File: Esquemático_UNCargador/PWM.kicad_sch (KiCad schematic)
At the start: 10 parts, among them U1 LM324N

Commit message: Se modifica esquema del micro y se agrega página de sensores
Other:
- note added: "VERIFICAR ESTE COMPONENTE"
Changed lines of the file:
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@@
+    (stroke (width 0) (type default))
+  )
+  (wire (pts (xy 85.09 30.48) (xy 86.36 30.48))
     (stroke (width 0) (type default))
   )
@@
     (stroke (width 0) (type default))
   )
-  (wire (pts (xy 85.09 30.48) (xy 85.598 30.48))
-    (stroke (width 0) (type default))
-  )
   (wire (pts (xy 120.65 73.66) (xy 120.65 72.39))
     (stroke (width 0) (type default))
   )
+  (wire (pts (xy 86.36 26.67) (xy 86.36 30.48))
+    (stroke (width 0) (type default))
+  )
   (wire (pts (xy 137.16 58.42) (xy 140.97 58.42))
     (stroke (width 0) (type default))
@@
     (stroke (width 0) (type default))
   )
+  (wire (pts (xy 26.67 59.69) (xy 26.67 70.866))
+    (stroke (width 0) (type default))
+  )
+  (wire (pts (xy 137.16 57.15) (xy 137.16 58.42))
+    (stroke (width 0) (type default))
+  )
+  (wire (pts (xy 140.97 58.42) (xy 149.86 58.42))
+    (stroke (width 0) (type default))
+  )
   (wire (pts (xy 78.74 30.48) (xy 85.09 30.48))
     (stroke (width 0) (type default))
   )
-  (wire (pts (xy 26.67 59.69) (xy 26.67 70.866))
-    (stroke (width 0) (type default))
-  )
-  (wire (pts (xy 137.16 57.15) (xy 137.16 58.42))
-    (stroke (width 0) (type default))
-  )
-  (wire (pts (xy 140.97 58.42) (xy 149.86 58.42))
-    (stroke (width 0) (type default))
-  )
   (wire (pts (xy 104.14 57.15) (xy 137.16 57.15))
     (stroke (width 0) (type default))
@@
   (wire (pts (xy 123.19 73.66) (xy 120.65 73.66))
     (stroke (width 0) (type default))
+  )
+  (text "VERIFICAR \nESTE \nCOMPONENTE" (at 144.78 69.85 0)
+    (effects (font (size 1.2 1.2) (color 255 14 46 1)) (justify left bottom))
   )
   (global_label "Pilot_ADC" (shape output) (at 123.19 73.66 0) (fields_autoplaced)
@@
     )
   )
-  (symbol (lib_id "power:+12V") (at 85.09 30.48 0) (unit 1)
-    (in_bom yes) (on_board yes) (dnp no) (fields_autoplaced)
-    (property "Reference" "#PWR0101" (at 85.09 34.29 0)
-      (effects (font (size 1.27 1.27)) hide)
-    )
-    (property "Value" "+12V" (at 85.09 25.146 0)
-      (effects (font (size 1.27 1.27)))
-    )
-    (property "Footprint" "" (at 85.09 30.48 0)
-      (effects (font (size 1.27 1.27)) hide)
-    )
-    (property "Datasheet" "" (at 85.09 30.48 0)
-      (effects (font (size 1.27 1.27)) hide)
-    )
+  (symbol (lib_id "power:+12V") (at 86.36 26.67 0) (unit 1)
+    (in_bom yes) (on_board yes) (dnp no) (fields_autoplaced)
+    (property "Reference" "#PWR0101" (at 86.36 30.48 0)
+      (effects (font (size 1.27 1.27)) hide)
+    )
+    (property "Value" "+12V" (at 86.36 21.336 0)
+      (effects (font (size 1.27 1.27)))
+    )
+    (property "Footprint" "" (at 86.36 26.67 0)
+      (effects (font (size 1.27 1.27)) hide)
+    )
+    (property "Datasheet" "" (at 86.36 26.67 0)
+      (effects (font (size 1.27 1.27)) hide)
+    )

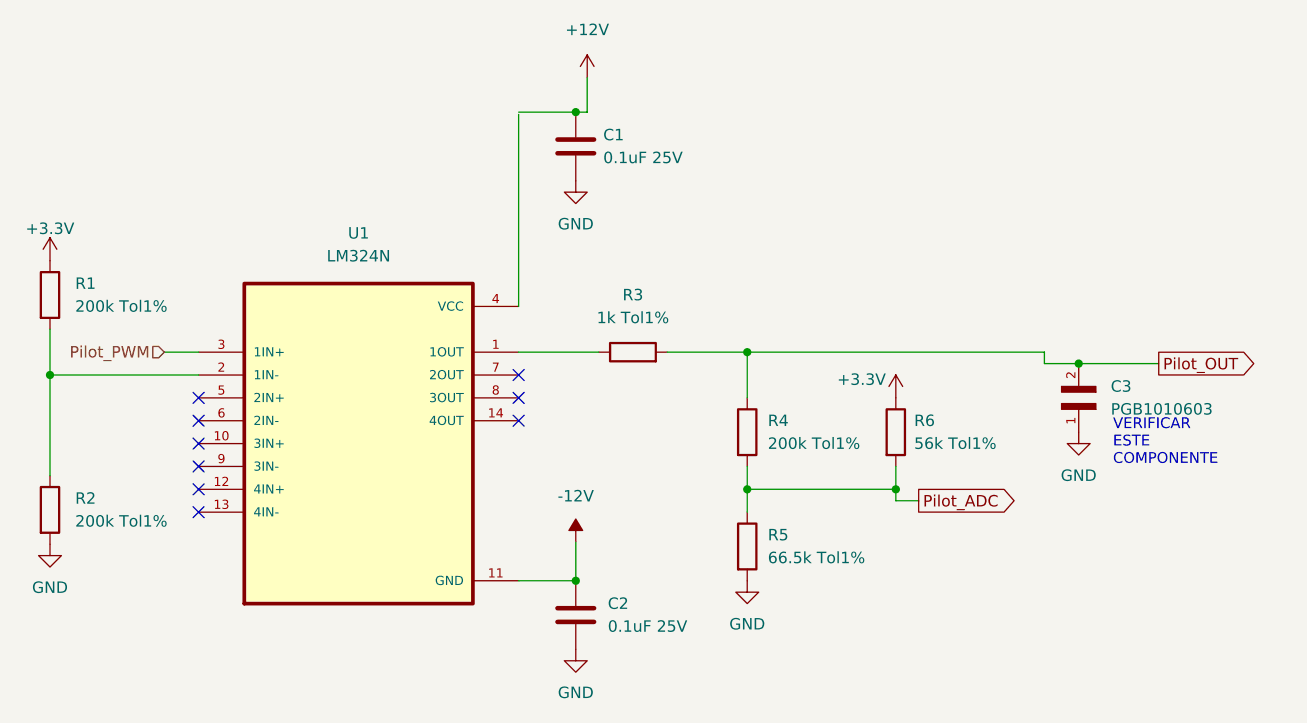
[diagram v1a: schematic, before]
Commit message: Avances en Huellas
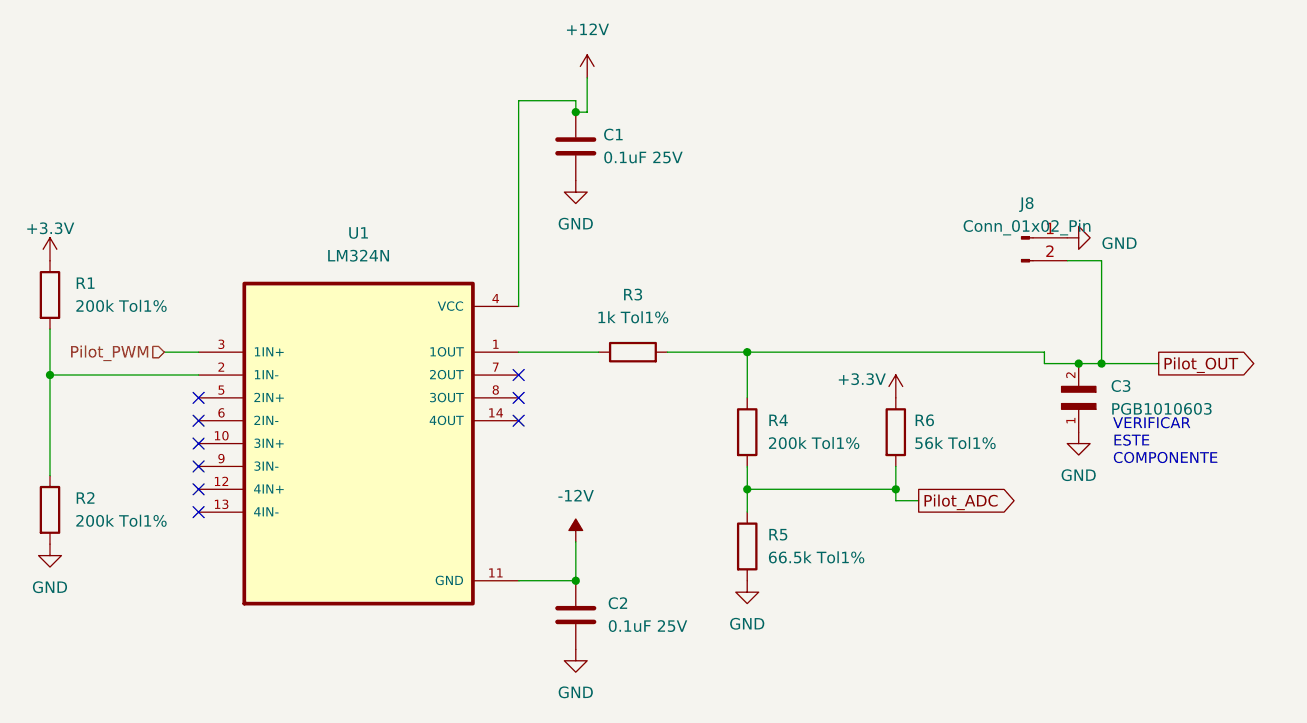
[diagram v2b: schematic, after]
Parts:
- added J8: Conn_01x02_Pin, TerminalBlock:TerminalBlock_Wuerth_691311400102_P7.62mm, symbol Connector:Conn_01x02_Pin
- C3: footprint symbols-footprints:ESD_PGB1010603MR -> Resistor_SMD:R_0603_1608Metric_Pad0.98x0.95mm_HandSolder
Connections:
- net +12V: now also U1.4 (VCC)
- net GND: now also J8.1 (Pin_1)
- net Pilot_OUT: now also J8.2 (Pin_2)
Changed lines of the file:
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@@
   (junction (at 120.65 72.39) (diameter 0) (color 0 0 0 0)
+  )
+  (junction (at 143.51 58.42) (diameter 0) (color 0 0 0 0)
   )
   (junction (at 104.14 57.15) (diameter 0) (color 0 0 0 0)
@@
     (stroke (width 0) (type default))
   )
+  (wire (pts (xy 143.51 58.42) (xy 143.51 46.99))
+    (stroke (width 0) (type default))
+  )
   (wire (pts (xy 85.09 30.48) (xy 86.36 30.48))
     (stroke (width 0) (type default))
@@
     (stroke (width 0) (type default))
   )
-  (wire (pts (xy 78.74 52.07) (xy 78.74 30.734))
+  (wire (pts (xy 78.74 52.07) (xy 78.74 29.21))
+    (stroke (width 0) (type default))
+  )
+  (wire (pts (xy 143.51 58.42) (xy 149.86 58.42))
+    (stroke (width 0) (type default))
+  )
+  (wire (pts (xy 85.09 29.21) (xy 85.09 30.48))
     (stroke (width 0) (type default))
   )
@@
     (stroke (width 0) (type default))
   )
+  (wire (pts (xy 143.51 46.99) (xy 139.7 46.99))
+    (stroke (width 0) (type default))
+  )
   (wire (pts (xy 78.74 82.55) (xy 85.09 82.55))
     (stroke (width 0) (type default))
@@
     (stroke (width 0) (type default))
   )
-  (wire (pts (xy 140.97 58.42) (xy 149.86 58.42))
-    (stroke (width 0) (type default))
-  )
-  (wire (pts (xy 78.74 30.48) (xy 85.09 30.48))
+  (wire (pts (xy 140.97 58.42) (xy 143.51 58.42))
+    (stroke (width 0) (type default))
+  )
+  (wire (pts (xy 78.74 29.21) (xy 85.09 29.21))
     (stroke (width 0) (type default))
   )
@@
       (effects (font (size 1.27 1.27)) (justify right))
     )
-    (property "Footprint" "symbols-footprints:ESD_PGB1010603MR" (at 140.97 63.5 0)
+    (property "Footprint" "Resistor_SMD:R_0603_1608Metric_Pad0.98x0.95mm_HandSolder" (at 140.97 63.5 0)
       (effects (font (size 1.27 1.27)) (justify bottom) hide)
     )
@@
         (path "/f64e4c48-29c2-4644-b6e3-d55b9152fc29/758fec3f-d66e-4356-8861-1c58650d5bb5"
           (reference "R4") (unit 1)
+        )
+      )
+    )
+  )
+  (symbol (lib_id "Connector:Conn_01x02_Pin") (at 134.62 44.45 0) (unit 1)
+    (in_bom yes) (on_board yes) (dnp no) (fields_autoplaced)
+    (property "Reference" "J8" (at 135.255 40.64 0)
+      (effects (font (size 1.27 1.27)))
+    )
+    (property "Value" "Conn_01x02_Pin" (at 135.255 43.18 0)
+      (effects (font (size 1.27 1.27)))
+    )
+    (property "Footprint" "TerminalBlock:TerminalBlock_Wuerth_691311400102_P7.62mm" (at 134.62 44.45 0)
+      (effects (font (size 1.27 1.27)) hide)
+    )
+    (property "Datasheet" "~" (at 134.62 44.45 0)
+      (effects (font (size 1.27 1.27)) hide)
+    )
+    (pin "1")
+    (pin "2")
+    (instances
+      (project "CircuitoPotencia"
+        (path "/f64e4c48-29c2-4644-b6e3-d55b9152fc29/758fec3f-d66e-4356-8861-1c58650d5bb5"
+          (reference "J8") (unit 1)
         )
       )
@@
         )
       )
+    )
+  )
+  (symbol (lib_name "GND_1") (lib_id "power:GND") (at 139.7 44.45 90) (unit 1)
+    (in_bom yes) (on_board yes) (dnp no) (fields_autoplaced)
+    (property "Reference" "#PWR035" (at 146.05 44.45 0)
+      (effects (font (size 1.27 1.27)) hide)
+    )
+    (property "Value" "GND" (at 143.51 45.085 90)
+      (effects (font (size 1.27 1.27)) (justify right))
+    )
+    (property "Footprint" "" (at 139.7 44.45 0)
+      (effects (font (size 1.27 1.27)) hide)
+    )
+    (property "Datasheet" "" (at 139.7 44.45 0)
+      (effects (font (size 1.27 1.27)) hide)
+    )
+    (pin "1")
+    (instances
+      (project "CircuitoPotencia"
+        (path "/f64e4c48-29c2-4644-b6e3-d55b9152fc29/758fec3f-d66e-4356-8861-1c58650d5bb5"
+          (reference "#PWR035") (unit 1)
+        )
+      )

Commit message: version inicial layout PCB
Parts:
- U1: footprint symbols-footprints:DIP794W45P254L1969H508Q14 -> LM324:DIP794W45P254L1969H508Q14
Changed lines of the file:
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@@
       (effects (font (size 1.27 1.27)))
     )
-    (property "Footprint" "symbols-footprints:DIP794W45P254L1969H508Q14" (at 60.96 67.31 0)
+    (property "Footprint" "LM324:DIP794W45P254L1969H508Q14" (at 60.96 67.31 0)
       (effects (font (size 1.27 1.27)) (justify bottom) hide)
     )

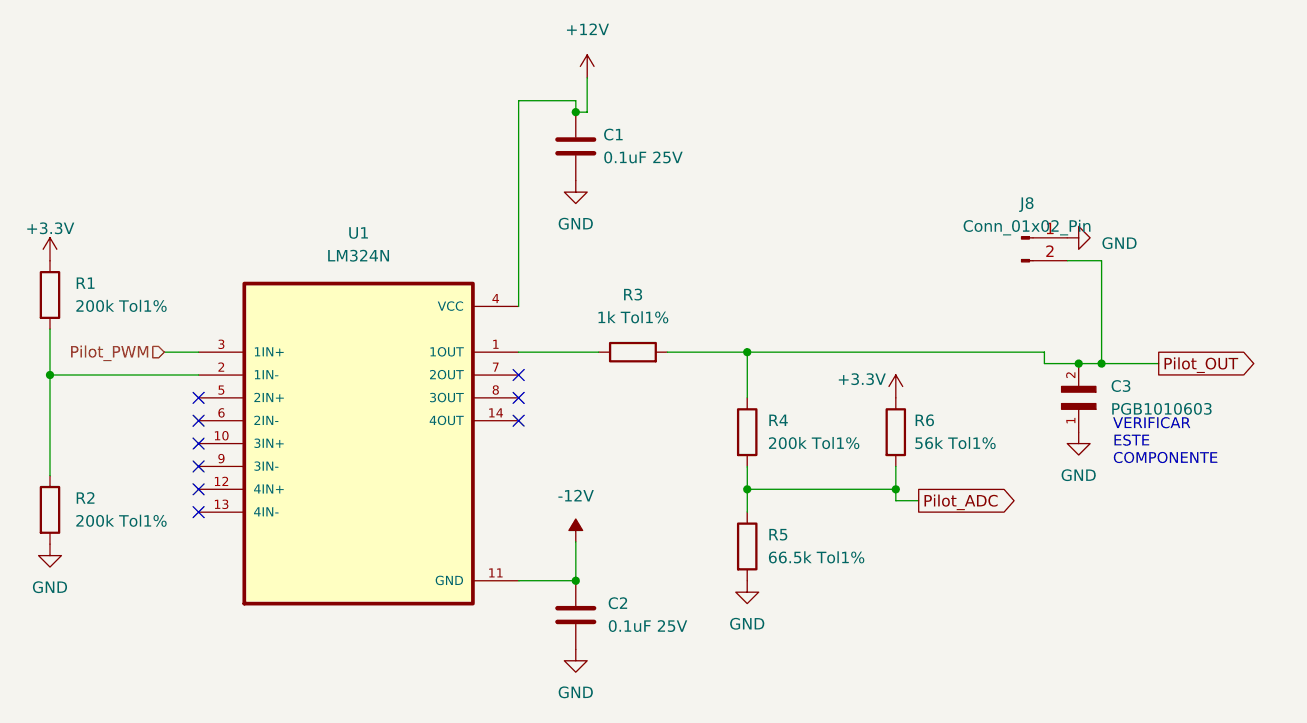
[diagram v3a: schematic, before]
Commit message: PCB con ruteo realizado. Errores en los anchos de vias -0.2mm. Huella LF356n actualizada
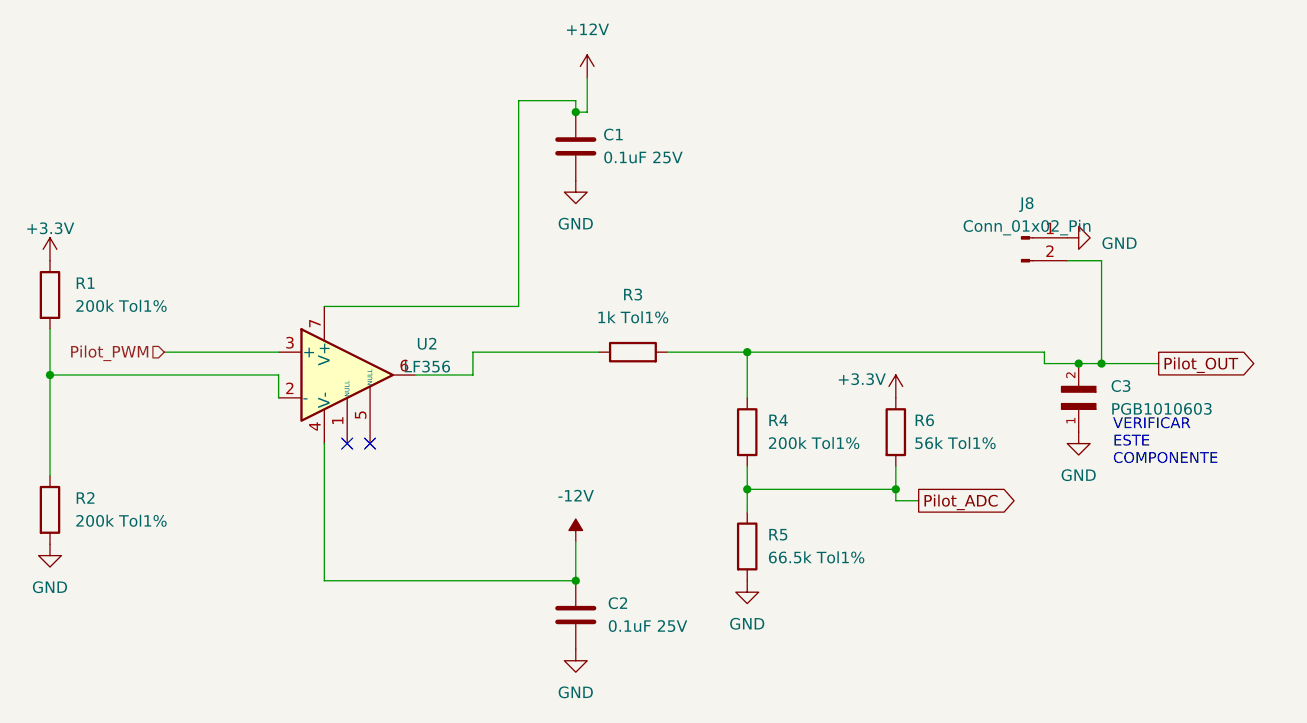
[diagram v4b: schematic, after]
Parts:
- removed U1: LM324N, LM324:DIP794W45P254L1969H508Q14, symbol LM324N:LM324N
- added U2: LF356, LF353:DIL08, symbol Amplifier_Operational:LF356
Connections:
- net +12V: now also U2.7 (V+)
- net -12V: now also U2.4 (V-)
- net Pilot_PWM: now also U2.3 (+)
- net at R3.1: now also U2.6
- net at R1.2, R2.1: now also U2.2 (-)
- no-connect marks 9 -> 2
